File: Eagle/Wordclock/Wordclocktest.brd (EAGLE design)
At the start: 160 x 100 mm, 21 parts, among them IC1 74HC595D, IC5 74HC595D

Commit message: WS2812 Layout versucht
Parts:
- removed IC1, IC5: 74HC595D, 74xx-eu:SO16
- removed LED1, LED2, LED3, LED4, LED5, LED6, LED7, LED8: (no value), led:SMARTLED-TTW
- removed Q1: (no value), special:Q
- removed R1, R2, R3, R4, R5, R6, R7, R8: (no value), resistor:MINI_MELF-0102W
- removed S+1: DS1337+, eagle-library-edeca.net-v5:DIL8
- removed U$1: MINI-USB, eagle-library-edeca.net-v5:MINI-USB
- added C1, C10, C2, C3, C4, C5, C6, C7, C8, C9: 100n, rcl:C1310
- added L1, L10, L11, L2, L3, L4, L5, L6, L7, L8, L9: WS2812B, adafruit:WS2812B
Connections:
- removed net N$11: LED1.C@1, R1.1
- removed net N$12: LED2.C@1, R2.1
- removed net N$13: LED3.C@1, R3.1
- removed net N$14: LED5.C@1, R5.1
- removed net N$15: LED6.C@1, R6.1
- removed net N$16: LED7.C@1, R7.1
- removed net N$17: R1.2, R2.2, R3.2, R4.2, R5.2, R6.2, R7.2, R8.2
- removed net N$18: IC5.14
- removed net N$19: IC5.9
- removed net VCC: IC1.16
- removed net VDD: IC5.16
- new net OUTROW1: L11.2-DOUT
- net +5V: now also C1.1, C10.1, C2.1, C3.1, C4.1, C5.1, C6.1, C7.1, C8.1, C9.1, L1.1-VDD, L10.1-VDD, L11.1-VDD, L2.1-VDD, L3.1-VDD, L4.1-VDD, L5.1-VDD, L6.1-VDD, L7.1-VDD, L8.1-VDD, L9.1-VDD; no longer U$1.1
- net GND: now also C1.2, C10.2, C2.2, C3.2, C4.2, C5.2, C6.2, C7.2, C8.2, C9.2, L1.3-GND, L10.3-GND, L11.3-GND, L2.3-GND, L3.3-GND, L4.3-GND, L5.3-GND, L6.3-GND, L7.3-GND, L8.3-GND, L9.3-GND; no longer IC1.8, IC5.8, U$1.5
- net N$1: now also L1.2-DOUT, L2.4-DIN; no longer IC5.4, LED5.A@1
- net N$10: now also L10.2-DOUT, L11.4-DIN; no longer LED8.C@1, R8.1
- net N$2: now also L2.2-DOUT, L3.4-DIN; no longer IC5.5, LED6.A@1
- net N$3: now also L3.2-DOUT, L4.4-DIN; no longer IC5.6, LED7.A@1
- net N$4: now also L4.2-DOUT, L5.4-DIN; no longer IC5.7, LED8.A@1
- net N$5: now also L6.2-DOUT, L7.4-DIN; no longer IC5.3, LED4.A@1
- net N$6: now also L5.2-DOUT, L6.4-DIN; no longer IC5.2, LED3.A@1
- net N$7: now also L7.2-DOUT, L8.4-DIN; no longer IC5.1, LED2.A@1
- net N$8: now also L8.2-DOUT, L9.4-DIN; no longer IC5.15, LED1.A@1
- net N$9: now also L10.4-DIN, L9.2-DOUT; no longer LED4.C@1, R4.1
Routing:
- net GND: track 0.00 -> 69.5 mm
- net N$1: track 0.00 -> 6.63 mm
- net N$4: track 0.00 -> 6.63 mm
- net N$3: track 0.00 -> 6.63 mm
- net N$2: track 0.00 -> 6.63 mm

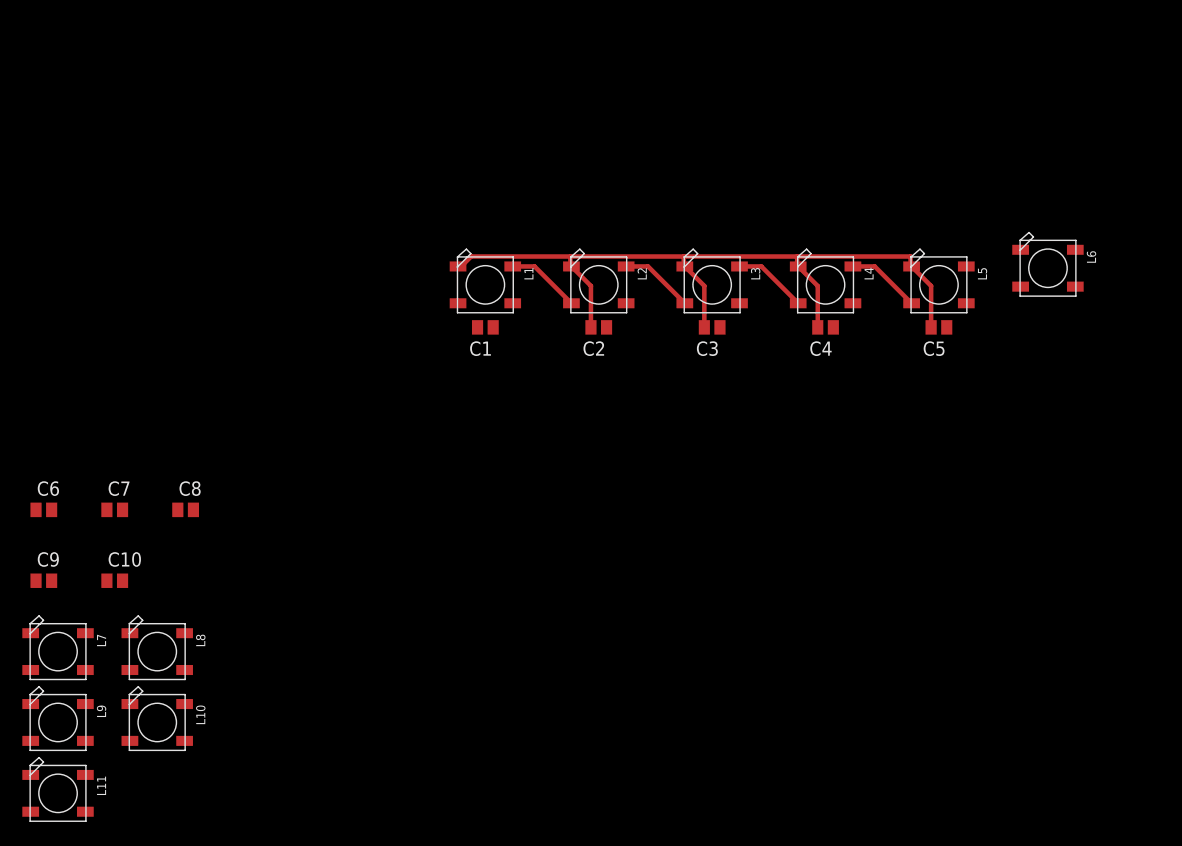
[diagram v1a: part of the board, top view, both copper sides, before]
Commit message: CAD Frontplattendesign eingefügt
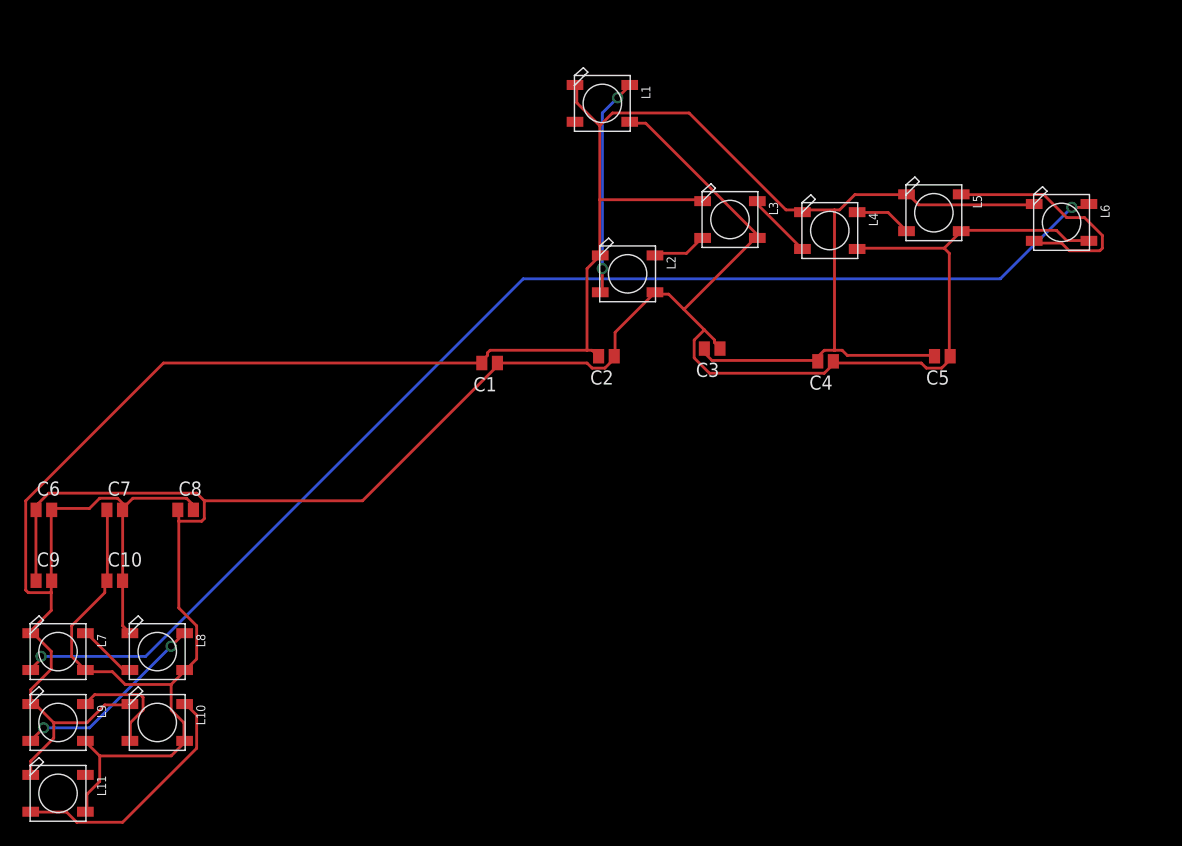
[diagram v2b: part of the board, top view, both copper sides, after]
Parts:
- moved L1 19.3 mm to (-16.0, -22.0)
- moved L5 6.48 mm to (13.7, -31.8)
- moved L3 6.07 mm to (-4.56, -32.4)
- moved L4 4.88 mm to (4.38, -33.4)
- moved L6 4.28 mm to (25.1, -32.7)
- moved C1 3.22 mm to (-26.1, -45.3)
- moved C4 3.04 mm to (4.00, -45.1)
- moved L2 2.77 mm to (-13.7, -37.3)
- moved C2 2.67 mm to (-15.6, -44.7)
- moved C5 2.60 mm to (14.5, -44.7)
- moved C3 1.90 mm to (-6.16, -44.0)
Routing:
- net +5V: track 0.00 -> 232.9 mm
- net GND: track 69.5 -> 244.1 mm
- net N$5: track 0.00 -> 112.3 mm, vias 0 -> 2
- net N$10: track 0.00 -> 22.5 mm
- net N$6: track 0.00 -> 21.9 mm
- net N$8: track 0.00 -> 17.8 mm, vias 0 -> 2
- net N$1: track 6.63 -> 19.7 mm, vias 0 -> 2
- net N$9: track 0.00 -> 10.0 mm
- net N$7: track 0.00 -> 5.33 mm
- net N$2: track 6.63 -> 4.96 mm
- net N$4: track 6.63 -> 5.14 mm

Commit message: Wordclock Matrix gelayoutet
Matrix alle Zeilen einzeln gelautet, Zeilen sind noch nicht verbunden
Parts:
- added C11, C12, C13, C14, C15, C16, C17, C18, C19, C20, C21, C22, C23, C24, C25, C26, C27, C28, C29, C30, C31, C32, C33: 100n, rcl:C1310
- added L12, L13, L14, L15, L16, L17, L18, L19, L20, L21, L22, L23, L24, L25, L26, L27, L28, L29, L30, L31, L32, L33: WS2812B, adafruit:WS2812B
- added LED1, LED2, LED3, LED4, LED5, LED6: (no value), led:CHIP-LED0603
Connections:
- new net N$11: L12.2-DOUT, L13.4-DIN
- new net N$12: L1.4-DIN, LED1.A
- new net N$13: L13.2-DOUT, L14.4-DIN
- new net N$14: L14.2-DOUT, L15.4-DIN
- new net N$15: L15.2-DOUT, L16.4-DIN
- new net N$16: L16.2-DOUT, L17.4-DIN
- new net N$17: L17.2-DOUT, L18.4-DIN
- new net N$18: L18.2-DOUT, L19.4-DIN
- new net N$19: L19.2-DOUT, L20.4-DIN
- new net N$20: L20.2-DOUT, L21.4-DIN
- new net N$21: L21.2-DOUT, L22.4-DIN
- new net N$22: L12.4-DIN, LED3.A
- new net N$23: L23.2-DOUT, L24.4-DIN
- new net N$24: L24.2-DOUT, L25.4-DIN
- new net N$25: L25.2-DOUT, L26.4-DIN
- new net N$26: L26.2-DOUT, L27.4-DIN
- new net N$27: L27.2-DOUT, L28.4-DIN
- new net N$28: L28.2-DOUT, L29.4-DIN
- new net N$29: L29.2-DOUT, L30.4-DIN
- new net N$30: L30.2-DOUT, L31.4-DIN
- new net N$31: L31.2-DOUT, L32.4-DIN
- new net N$32: L32.2-DOUT, L33.4-DIN
- new net N$33: L23.4-DIN, LED5.A
- new net OUTROW2: L22.2-DOUT, LED4.C
- new net OUTROW3: L33.2-DOUT, LED6.C
- net +5V: now also C11.1, C12.1, C13.1, C14.1, C15.1, C16.1, C17.1, C18.1, C19.1, C20.1, C21.1, C22.1, C23.1, C24.1, C25.1, C26.1, C27.1, C28.1, C29.1, C30.1, C31.1, C32.1, C33.1, L12.1-VDD, L13.1-VDD, L14.1-VDD, L15.1-VDD, L16.1-VDD, L17.1-VDD, L18.1-VDD, L19.1-VDD, L20.1-VDD, L21.1-VDD, L22.1-VDD, L23.1-VDD, L24.1-VDD, L25.1-VDD, L26.1-VDD, L27.1-VDD, L28.1-VDD, L29.1-VDD, L30.1-VDD, L31.1-VDD, L32.1-VDD, L33.1-VDD, LED2.A, LED4.A, LED6.A
- net GND: now also C11.2, C12.2, C13.2, C14.2, C15.2, C16.2, C17.2, C18.2, C19.2, C20.2, C21.2, C22.2, C23.2, C24.2, C25.2, C26.2, C27.2, C28.2, C29.2, C30.2, C31.2, C32.2, C33.2, L12.3-GND, L13.3-GND, L14.3-GND, L15.3-GND, L16.3-GND, L17.3-GND, L18.3-GND, L19.3-GND, L20.3-GND, L21.3-GND, L22.3-GND, L23.3-GND, L24.3-GND, L25.3-GND, L26.3-GND, L27.3-GND, L28.3-GND, L29.3-GND, L30.3-GND, L31.3-GND, L32.3-GND, L33.3-GND, LED1.C, LED3.C, LED5.C
- net OUTROW1: now also LED2.C
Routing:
- net +5V: track 232.9 -> 982.2 mm, vias 0 -> 1
- net GND: track 244.1 -> 967.4 mm
- net N$33: track 0.00 -> 129.0 mm
- net N$22: track 0.00 -> 129.0 mm
- net N$12: track 0.00 -> 129.0 mm
- net N$28: track 0.00 -> 112.3 mm, vias 0 -> 2
- net N$17: track 0.00 -> 112.3 mm, vias 0 -> 2
- net N$32: track 0.00 -> 22.5 mm
- net N$21: track 0.00 -> 22.5 mm
- net N$27: track 0.00 -> 21.9 mm
- net N$16: track 0.00 -> 21.9 mm
- net N$11: track 0.00 -> 19.7 mm, vias 0 -> 2
- net N$23: track 0.00 -> 19.7 mm, vias 0 -> 2
- net N$19: track 0.00 -> 17.8 mm, vias 0 -> 2
- net N$30: track 0.00 -> 17.8 mm, vias 0 -> 2
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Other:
- board size 160 x 100 mm -> 284.7 x 190.7 mm
